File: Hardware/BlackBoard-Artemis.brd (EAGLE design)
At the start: 68.6 x 53.3 mm, 114 parts, among them IC3 LM1117, J2 CORTEX_DEBUG, J3 POWER_JACKTOE, J5 USB-C, Q1 1.1A/60V/600mΩ, U1 ARTEMIS_MODULESMD, U3 AP2112-3.3V, U5 CH340C, Y1 32.768kHz

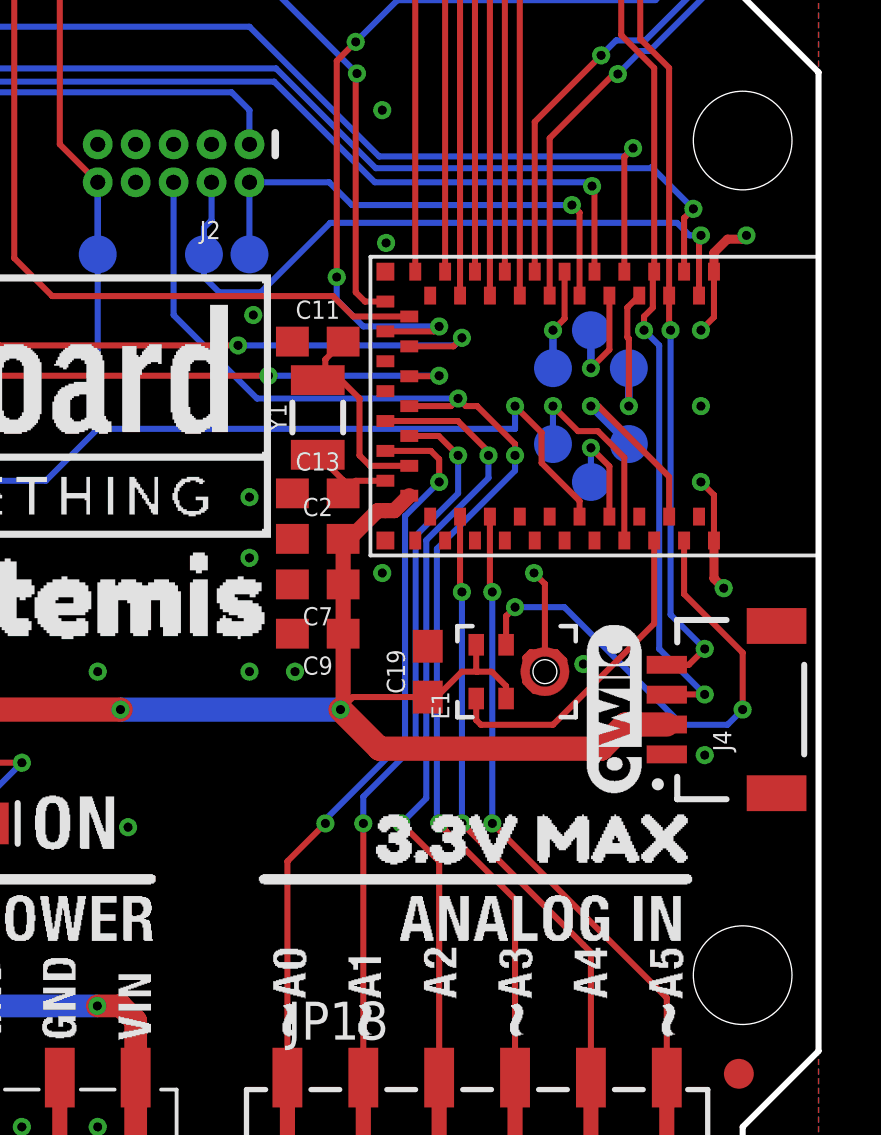
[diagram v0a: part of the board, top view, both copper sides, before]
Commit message: Move testpoint on BlackBoard
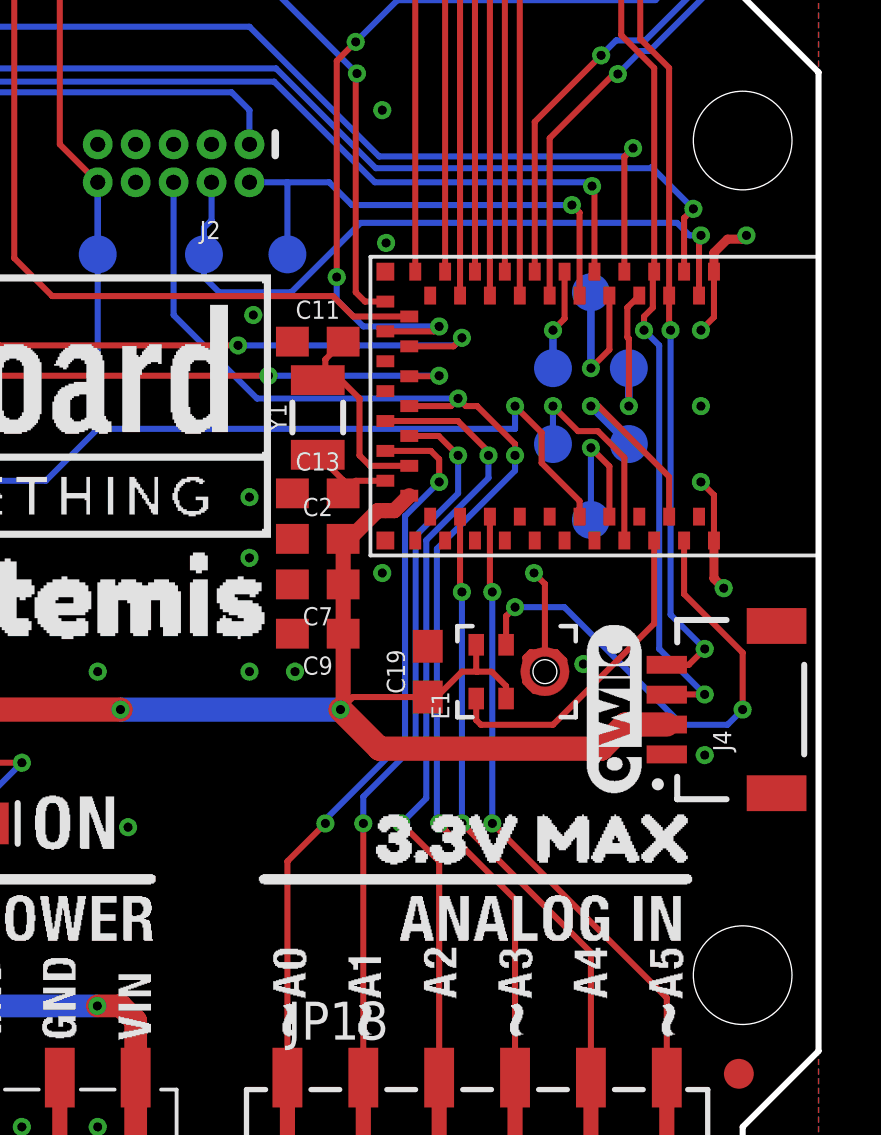
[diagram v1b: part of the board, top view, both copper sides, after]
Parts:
- moved TP14 1.27 mm to (61.0, 30.5)
- moved TP8 1.27 mm to (61.0, 22.9)
- moved U$19 1.27 mm to (63.2, 21.2)
- moved U$24 1.27 mm to (62.7, 32.1)
- moved TP2 1.27 mm to (50.8, 31.8)
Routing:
- net ~D29: track 3.70 -> 4.97 mm
- net D26: track 3.96 -> 5.23 mm
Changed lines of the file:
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@@
 <?xml version="1.0" encoding="utf-8"?>
 <!DOCTYPE eagle SYSTEM "eagle.dtd">
-<eagle version="9.3.0">
+<eagle version="9.4.0">
 <drawing>
 <settings>
@@
 <layer number="44" name="Drills" color="7" fill="1" visible="no" active="yes"/>
 <layer number="45" name="Holes" color="7" fill="1" visible="yes" active="yes"/>
-<layer number="46" name="Milling" color="3" fill="1" visible="no" active="yes"/>
+<layer number="46" name="Milling" color="3" fill="1" visible="yes" active="yes"/>
 <layer number="47" name="Measures" color="7" fill="1" visible="no" active="yes"/>
 <layer number="48" name="Document" color="7" fill="1" visible="no" active="yes"/>
@@
 <layer number="13" name="Route13" color="4" fill="5" visible="no" active="no"/>
 <layer number="14" name="Route14" color="1" fill="6" visible="no" active="no"/>
-<layer number="15" name="Route15" color="4" fill="6" visible="no" active="yes"/>
-<layer number="2" name="Route2" color="1" fill="3" visible="no" active="yes"/>
+<layer number="15" name="Route15" color="4" fill="6" visible="yes" active="yes"/>
+<layer number="2" name="Route2" color="1" fill="3" visible="yes" active="yes"/>
 <layer number="97" name="Info" color="7" fill="1" visible="no" active="no"/>
 <layer number="98" name="Guide" color="6" fill="1" visible="no" active="no"/>
@@
 </element>
 <element name="TP1" library="SparkFun-Connectors" package="PAD.03X.05" value="" x="48.006" y="31.75" smashed="yes" rot="MR90"/>
-<element name="TP2" library="SparkFun-Connectors" package="PAD.03X.05" value="" x="49.53" y="31.75" smashed="yes" rot="MR90"/>
+<element name="TP2" library="SparkFun-Connectors" package="PAD.03X.05" value="" x="50.8" y="31.75" smashed="yes" rot="MR90"/>
 <element name="J2" library="SparkFun-Connectors" package="2X5-PTH-1.27MM-NO_SILK" value="CORTEX_DEBUG" x="46.99" y="34.798" smashed="yes" rot="R180">
 <attribute name="NAME" x="48.5648" y="32.8676" size="0.6096" layer="25" font="vector" ratio="20" rot="R180"/>
@@
 </element>
 <element name="U1" library="Testing" package="ARTEMIS_FP" value="ARTEMIS_MODULESMD" x="60.579" y="26.67" smashed="yes"/>
-<element name="TP8" library="SparkFun-Connectors" package="PAD.03X.05" value="" x="60.96" y="24.13" smashed="yes" rot="MR270"/>
+<element name="TP8" library="SparkFun-Connectors" package="PAD.03X.05" value="" x="60.96" y="22.86" smashed="yes" rot="MR270"/>
 <element name="TP9" library="SparkFun-Connectors" package="PAD.03X.05" value="" x="59.69" y="25.4" smashed="yes" rot="MR270"/>
 <element name="TP11" library="SparkFun-Connectors" package="PAD.03X.05" value="" x="62.23" y="25.4" smashed="yes" rot="MR0"/>
 <element name="TP12" library="SparkFun-Connectors" package="PAD.03X.05" value="" x="59.69" y="27.94" smashed="yes" rot="MR0"/>
 <element name="TP13" library="SparkFun-Connectors" package="PAD.03X.05" value="" x="62.23" y="27.94" smashed="yes" rot="MR0"/>
-<element name="TP14" library="SparkFun-Connectors" package="PAD.03X.05" value="" x="60.96" y="29.21" smashed="yes" rot="MR0"/>
+<element name="TP14" library="SparkFun-Connectors" package="PAD.03X.05" value="" x="60.96" y="30.48" smashed="yes" rot="MR0"/>
 <element name="U$47" library="buzzard_labels (8)" package="MISO8" value="" x="31.496" y="42.545" smashed="yes" rot="R90"/>
 <element name="U$48" library="buzzard_labels (8)" package="MOSI7" value="" x="34.036" y="42.545" smashed="yes" rot="R90"/>
@@
 <element name="U$13" library="buzzard_labels (2)" package="3#3V_MAX2" value="" x="52.324" y="12.192" smashed="yes"/>
 <element name="U$17" library="buzzard_labels (2)" package="#284" value="" x="58.801" y="25.4" smashed="yes" rot="MR0"/>
-<element name="U$19" library="buzzard_labels (2)" package="#295" value="" x="63.246" y="22.479" smashed="yes" rot="MR0"/>
+<element name="U$19" library="buzzard_labels (2)" package="#295" value="" x="63.246" y="21.209" smashed="yes" rot="MR0"/>
 <element name="U$21" library="buzzard_labels (2)" package="240" value="" x="58.801" y="27.94" smashed="yes" rot="MR0"/>
 <element name="U$23" library="buzzard_labels (2)" package="251" value="" x="66.548" y="27.94" smashed="yes" rot="MR0"/>
-<element name="U$24" library="buzzard_labels (2)" package="262" value="" x="62.738" y="30.861" smashed="yes" rot="MR0"/>
+<element name="U$24" library="buzzard_labels (2)" package="262" value="" x="62.738" y="32.131" smashed="yes" rot="MR0"/>
 <element name="U$25" library="buzzard_labels (2)" package="273" value="" x="66.548" y="25.4" smashed="yes" rot="MR0"/>
 </elements>
@@
 <contactref element="TP2" pad="P$1"/>
 <contactref element="J2" pad="2"/>
-<wire x1="49.53" y1="34.163" x2="49.53" y2="31.75" width="0.2032" layer="16"/>
 <contactref element="U1" pad="SWDIO"/>
 <wire x1="60.325" y1="33.401" x2="60.579" y2="33.147" width="0.2032" layer="1"/>
@@
 <wire x1="60.325" y1="33.401" x2="52.959" y2="33.401" width="0.2032" layer="16"/>
 <wire x1="52.959" y1="33.401" x2="52.197" y2="34.163" width="0.2032" layer="16"/>
-<wire x1="52.197" y1="34.163" x2="49.53" y2="34.163" width="0.2032" layer="16"/>
+<wire x1="52.197" y1="34.163" x2="50.8" y2="34.163" width="0.2032" layer="16"/>
+<wire x1="50.8" y1="34.163" x2="49.53" y2="34.163" width="0.2032" layer="16"/>
+<wire x1="50.8" y1="31.75" x2="50.8" y2="34.163" width="0.2032" layer="16"/>
 </signal>
 <signal name="SWDCK">
@@
 <wire x1="64.579" y1="32.321" x2="64.643" y2="32.385" width="0.2032" layer="1"/>
 <via x="64.643" y="32.385" extent="1-16" drill="0.3048"/>
-<wire x1="52.2351" y1="32.8041" x2="49.911" y2="30.48" width="0.2032" layer="16"/>
+<wire x1="53.2511" y1="32.8041" x2="50.927" y2="30.48" width="0.2032" layer="16"/>
 <wire x1="64.643" y1="32.385" x2="64.262" y2="32.385" width="0.2032" layer="16"/>
 <wire x1="64.262" y1="32.385" x2="63.8429" y2="32.8041" width="0.2032" layer="16"/>
-<wire x1="63.8429" y1="32.8041" x2="52.2351" y2="32.8041" width="0.2032" layer="16"/>
-<wire x1="49.911" y1="30.48" x2="48.514" y2="30.48" width="0.2032" layer="16"/>
+<wire x1="63.8429" y1="32.8041" x2="53.2511" y2="32.8041" width="0.2032" layer="16"/>
+<wire x1="50.927" y1="30.48" x2="48.514" y2="30.48" width="0.2032" layer="16"/>
 <wire x1="48.514" y1="30.48" x2="48.006" y2="30.988" width="0.2032" layer="16"/>
 </signal>
@@
 <wire x1="61.579" y1="24.654" x2="60.96" y2="25.273" width="0.2032" layer="1"/>
 <via x="60.96" y="25.273" extent="1-16" drill="0.3048"/>
-<wire x1="60.96" y1="24.13" x2="60.96" y2="25.273" width="0.2032" layer="16"/>
+<wire x1="60.96" y1="22.86" x2="60.96" y2="25.273" width="0.2032" layer="16"/>
 </signal>
 <signal name="D24">
@@
 <wire x1="61.579" y1="28.559" x2="60.96" y2="27.94" width="0.2032" layer="1"/>
 <via x="60.96" y="27.94" extent="1-16" drill="0.3048"/>
-<wire x1="60.96" y1="29.21" x2="60.96" y2="27.94" width="0.254" layer="16"/>
+<wire x1="60.96" y1="30.48" x2="60.96" y2="27.94" width="0.254" layer="16"/>
 </signal>
 <signal name="D27">
@@
 <wire x1="56.642" y1="20.447" x2="56.642" y2="12.7" width="0.2032" layer="16"/>
 <via x="56.642" y="12.7" extent="1-16" drill="0.3048"/>
-<wire x1="56.642" y1="12.7" x2="60.706" y2="8.636" width="0.2032" layer="1"/>
+<wire x1="56.642" y1="12.7" x2="60.96" y2="8.382" width="0.2032" layer="1"/>
 <wire x1="60.96" y1="4.19" x2="60.96" y2="8.382" width="0.2032" layer="1"/>
-<wire x1="60.96" y1="8.382" x2="60.706" y2="8.636" width="0.2032" layer="1"/>
 </signal>
 </signals>
